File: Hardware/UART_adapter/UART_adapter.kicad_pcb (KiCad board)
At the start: 2 copper layers, 54 x 26.5 mm, 2 parts, among them J1 Conn_02x07_Top_Bottom

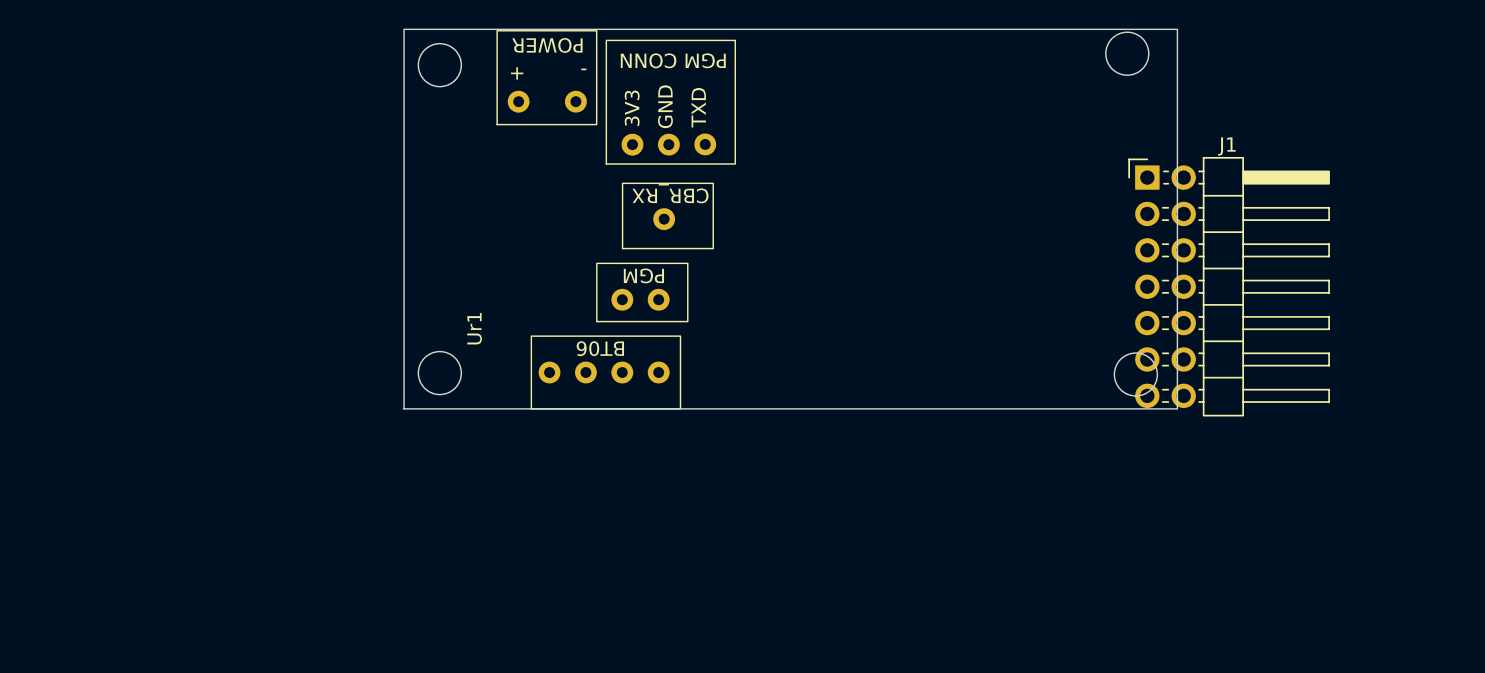
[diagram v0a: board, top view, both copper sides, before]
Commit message: Fixed USB traces, radio connectors, finished UART adapter
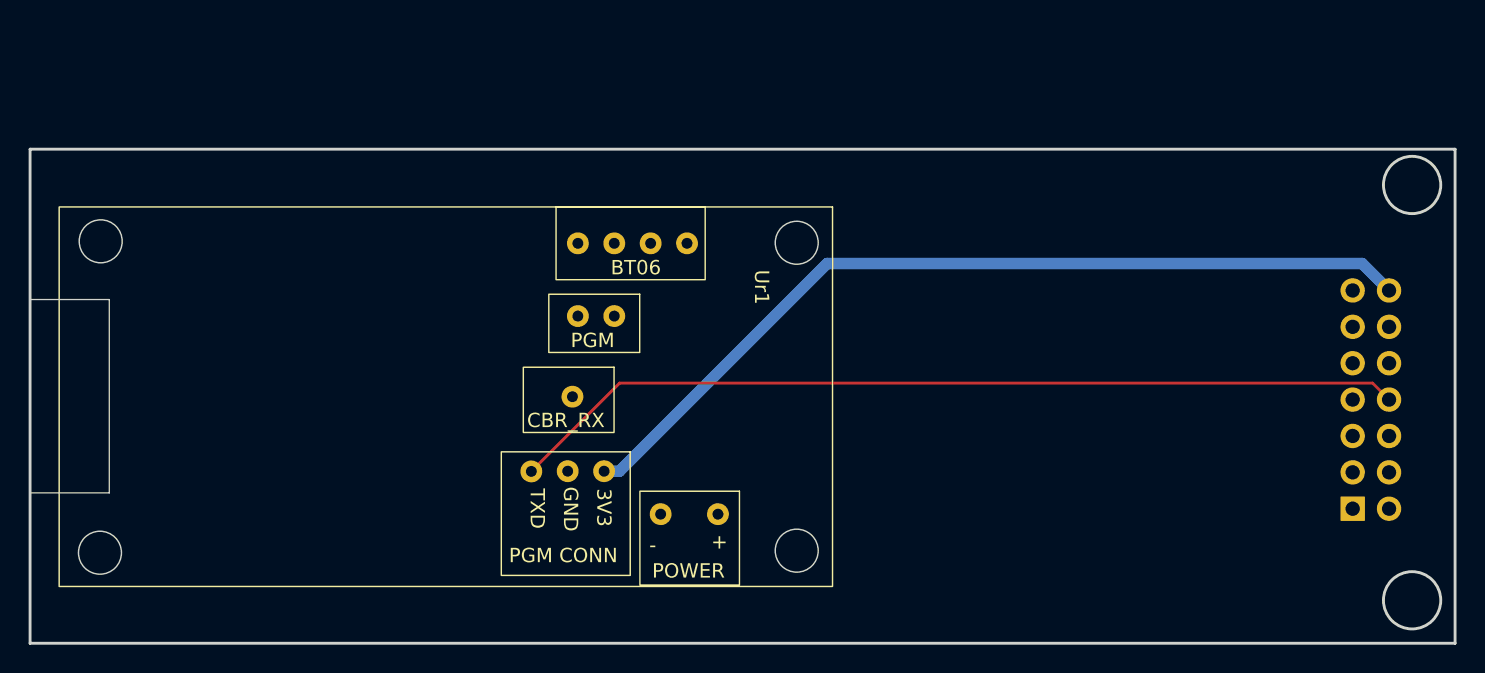
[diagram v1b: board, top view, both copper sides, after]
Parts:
- removed J1: Conn_02x07_Top_Bottom, Connector_PinHeader_2.54mm:PinHeader_2x07_P2.54mm_Horizontal
- added J2: Conn_02x07_Top_Bottom, Connector_PinHeader_2.54mm:PinHeader_2x07_P2.54mm_Horizontal, B.Cu at (185.3, 109.1)
- moved Ur1 33.1 mm to (149.0, 88.0), turned to -90 degrees
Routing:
- net /RADIO_RX: track 0.00 -> 62.9 mm
- net +3.3V: track 0.00 -> 61.6 mm
- added copper zone on B.Cu, net GND
- added copper zone on F.Cu, net GND
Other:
- board size 54 x 26.5 mm -> 99.5 x 34.5 mm
